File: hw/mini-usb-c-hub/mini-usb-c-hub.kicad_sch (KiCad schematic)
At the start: 30 parts, among them J101 USB_C_Receptacle_USB2.0_16P, P101 USB_C_Plug_USB3.0, U101 FE1.1s, Y101 12MHz

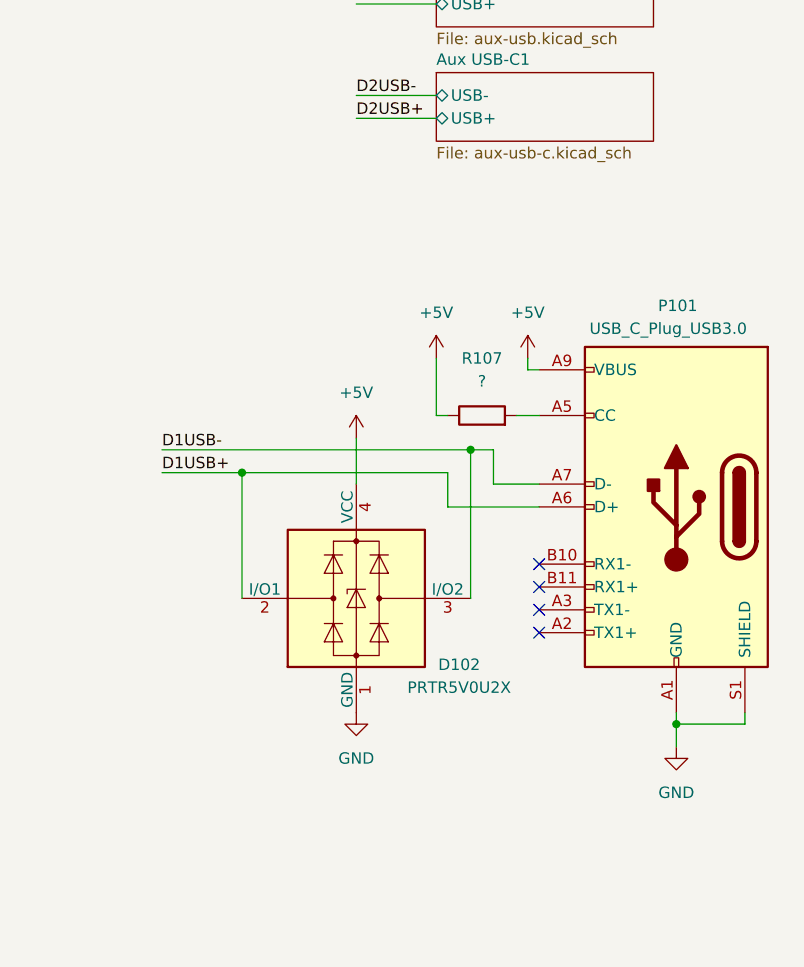
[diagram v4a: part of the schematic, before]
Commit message: chore(hw): replace USB-C plug with socket
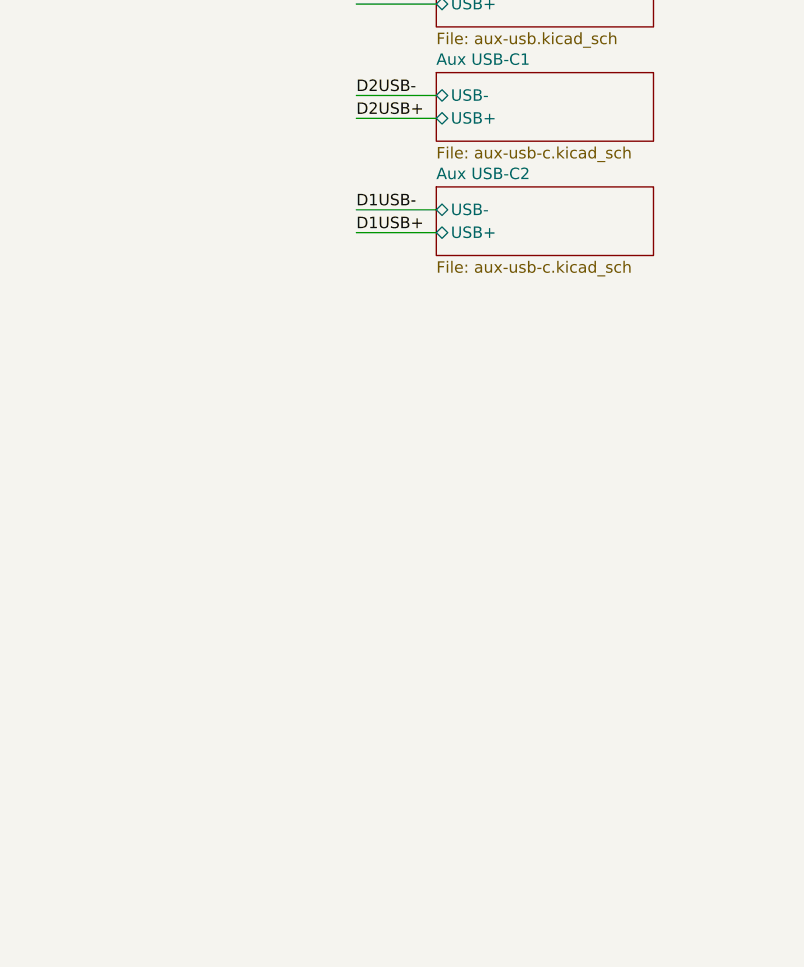
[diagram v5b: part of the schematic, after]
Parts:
- removed D102: PRTR5V0U2X, Package_TO_SOT_SMD:SOT-143, symbol Power_Protection:PRTR5V0U2X
- removed P101: USB_C_Plug_USB3.0, local:USB_C_Plug_G-Switch_GT-USB-8016A, symbol local:USB_C_Plug_USB3.0
- removed R107: ?, Resistor_SMD:R_0805_2012Metric_Pad1.20x1.40mm_HandSolder, symbol Device:R
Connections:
- no-connect marks 8 -> 4
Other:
- added sheet Aux USB-C2 (aux-usb-c.kicad_sch)

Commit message: chore(hw): update layout, fix references
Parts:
- added D101, D102, D104: LED, LED_SMD:LED_0805_2012Metric_Pad1.15x1.40mm_HandSolder, symbol Device:LED
- renumbered C108 to C102, C109 to C103, C106 to C104, C107 to C105, C102 to C106, C103 to C107, C104 to C108, C105 to C109, D104 to D105, D101 to D106, R114 to R101, R110 to R102, R112 to R103, R103 to R104, R101 to R105, R102 to R106, R106 to R107, R105 to R110, R104 to R112
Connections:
- net at D103.2 (A): now also R101.2, D101.1 (K); no longer R102.1
- net DRV: now reaches R103.1, U101.22 (DRV)
- net DRV: now also D103.1 (K), D101.2 (A), D102.2 (A), D104.1 (K); no longer R102.2
- net LED2: now reaches U101.24 (LED2)
- net LED2: now also R102.1; no longer D103.1 (K)
- net LED1: now reaches R101.1, U101.23 (LED1/EESCL)
- new net: D102.1 (K), D104.2 (A), R102.2
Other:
- note removed: "Should be 3v3?"
- moved on the sheet: D105, R101, R102, R103

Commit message: chore(hw): first complete layout
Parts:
- D101, D102, D103, D104, D105, R101, R102, R103: now not fitted
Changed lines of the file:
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@@
 		(in_bom yes)
 		(on_board yes)
-		(dnp no)
+		(dnp yes)
 		(property "Reference" "R102"
 			(at 212.09 129.54 90)
@@
 		(in_bom yes)
 		(on_board yes)
-		(dnp no)
+		(dnp yes)
 		(property "Reference" "D103"
 			(at 239.014 113.03 0)
@@
 		(in_bom yes)
 		(on_board yes)
-		(dnp no)
+		(dnp yes)
 		(property "Reference" "D104"
 			(at 239.014 133.35 0)
@@
 		(in_bom yes)
 		(on_board yes)
-		(dnp no)
+		(dnp yes)
 		(property "Reference" "D105"
 			(at 264.16 133.604 0)
@@
 		(in_bom yes)
 		(on_board yes)
-		(dnp no)
+		(dnp yes)
 		(property "Reference" "R103"
 			(at 262.89 121.92 90)
@@
 		(in_bom yes)
 		(on_board yes)
-		(dnp no)
+		(dnp yes)
 		(property "Reference" "D102"
 			(at 225.806 123.19 0)
@@
 		(in_bom yes)
 		(on_board yes)
-		(dnp no)
+		(dnp yes)
 		(property "Reference" "R101"
 			(at 212.09 109.22 90)
@@
 		(in_bom yes)
 		(on_board yes)
-		(dnp no)
+		(dnp yes)
 		(property "Reference" "D101"
 			(at 225.806 102.87 0)

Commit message: chore(hw): switch to KiCad 9.0
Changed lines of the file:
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@@
 (kicad_sch
-	(version 20231120)
+	(version 20250114)
 	(generator "eeschema")
-	(generator_version "8.0")
+	(generator_version "9.0")
 	(paper "A4")
+	(text "The capacitors and resistor should\nbe unpopulated when Revision B of\nthe chip is used"
+		(exclude_from_sim no)
+		(at 135.636 97.536 0)
+		(effects
+			(font
+				(size 1.27 1.27)
+			)
+		)
+	)
 	(junction
 		(at 104.14 115.57)
@@
 		)
 	)
-	(text "The capacitors and resistor should\nbe unpopulated when Revision B of\nthe chip is used"
-		(exclude_from_sim no)
-		(at 135.636 97.536 0)
-		(effects
-			(font
-				(size 1.27 1.27)
-			)
-		)
-	)
 	(label "D2USB-"
 		(at 142.24 138.43 180)
-		(fields_autoplaced yes)
 		(effects
 			(font
@@
 	(label "D2USB-"
 		(at 217.17 46.99 0)
-		(fields_autoplaced yes)
 		(effects
 			(font
@@
 	(label "D3USB+"
 		(at 142.24 143.51 180)
-		(fields_autoplaced yes)
 		(effects
 			(font
@@
 	(label "LED2"
 		(at 198.12 134.62 0)
-		(fields_autoplaced yes)
 		(effects
 			(font
@@
 	(label "UUSB-"
 		(at 88.9 135.89 0)
-		(fields_autoplaced yes)
 		(effects
 			(font
@@
 	(label "D4USB+"
 		(at 217.17 74.93 0)
-		(fields_autoplaced yes)
 		(effects
 			(font
@@
 	(label "D1USB+"
 		(at 217.17 36.83 0)
-		(fields_autoplaced yes)
 		(effects
 			(font
@@
 	(label "DRV"
 		(at 139.7 168.91 180)
-		(fields_autoplaced yes)
 		(effects
 			(font
@@
 	(label "D1USB+"
 		(at 142.24 128.27 180)
-		(fields_autoplaced yes)
 		(effects
 			(font
@@
 	(label "D4USB-"
 		(at 142.24 153.67 180)
-		(fields_autoplaced yes)
 		(effects
 			(font
@@
 	(label "D2USB+"
 		(at 142.24 135.89 180)
-		(fields_autoplaced yes)
 		(effects
 			(font
@@
 	(label "D3USB+"
 		(at 217.17 62.23 0)
-		(fields_autoplaced yes)
 		(effects
 			(font
@@
 	(label "LED1"
 		(at 139.7 163.83 180)
-		(fields_autoplaced yes)
 		(effects
 			(font
@@
 	(label "UUSB+"
 		(at 92.71 46.99 180)
-		(fields_autoplaced yes)
 		(effects
 			(font
@@
 	(label "D4USB-"
 		(at 217.17 72.39 0)
-		(fields_autoplaced yes)
 		(effects
 			(font
@@
 	(label "LED2"
 		(at 139.7 166.37 180)
-		(fields_autoplaced yes)
 		(effects
 			(font
@@
 	(label "D4USB+"
 		(at 142.24 151.13 180)
-		(fields_autoplaced yes)
 		(effects
 			(font
@@
 	(label "D2USB+"
 		(at 217.17 49.53 0)
-		(fields_autoplaced yes)
 		(effects
 			(font
@@
 	(label "D3USB-"
 		(at 142.24 146.05 180)
-		(fields_autoplaced yes)
 		(effects
 			(font
@@
 	(label "D3USB-"
 		(at 217.17 59.69 0)
-		(fields_autoplaced yes)
 		(effects
 			(font
@@
 	(label "UUSB-"
 		(at 92.71 44.45 180)
-		(fields_autoplaced yes)
 		(effects
 			(font
@@
 	(label "D1USB-"
 		(at 217.17 34.29 0)
-		(fields_autoplaced yes)
 		(effects
 			(font
@@
 	(label "UUSB+"
 		(at 88.9 133.35 0)
-		(fields_autoplaced yes)
 		(effects
 			(font
@@
 	(label "LED1"
 		(at 198.12 114.3 0)
-		(fields_autoplaced yes)
 		(effects
 			(font
@@
 	(label "DRV"
 		(at 198.12 146.05 0)
-		(fields_autoplaced yes)
 		(effects
 			(font
@@
 	(label "D1USB-"
 		(at 142.24 130.81 180)
-		(fields_autoplaced yes)
 		(effects
 			(font
@@
 		(at 226.06 31.75)
 		(size 24.13 7.62)
+		(exclude_from_sim no)
+		(in_bom yes)
+		(on_board yes)
+		(dnp no)
 		(fields_autoplaced yes)
 		(stroke
@@
 		(at 226.06 69.85)
 		(size 24.13 7.62)
+		(exclude_from_sim no)
+		(in_bom yes)
+		(on_board yes)
+		(dnp no)
 		(fields_autoplaced yes)
 		(stroke
@@
 		(at 226.06 57.15)
 		(size 24.13 7.62)
+		(exclude_from_sim no)
+		(in_bom yes)
+		(on_board yes)
+		(dnp no)
 		(fields_autoplaced yes)
 		(stroke
@@
 		(at 226.06 44.45)
 		(size 24.13 7.62)
+		(exclude_from_sim no)
+		(in_bom yes)
+		(on_board yes)
+		(dnp no)
 		(fields_autoplaced yes)
 		(stroke
@@
 		)
 	)
+	(embedded_fonts no)
 )
